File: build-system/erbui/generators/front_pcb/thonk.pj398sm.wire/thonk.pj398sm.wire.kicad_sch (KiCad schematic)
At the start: 4 parts, among them J1 IN

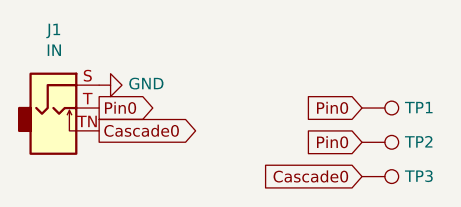
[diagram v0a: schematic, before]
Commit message: Replace cascade feature with normalling feature
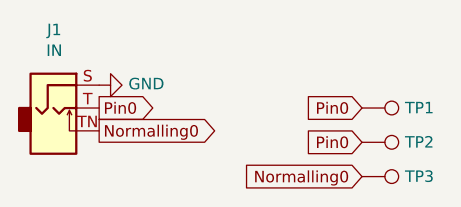
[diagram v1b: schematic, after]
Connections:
- net Cascade0 renamed Normalling0
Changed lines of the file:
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@@
 (kicad_sch (version 20211123) (generator eeschema)
   (paper "A4")
-  (global_label "Cascade0" (shape input) (at 127 114.3 180) (fields_autoplaced)
+  (global_label "Normalling0" (shape input) (at 127 114.3 180) (fields_autoplaced)
     (effects (font (size 1.27 1.27)) (justify right))
-    (property "Intersheet References" "${INTERSHEET_REFS}" (id 0) (at 0 0 0)
-      (effects (font (size 1.27 1.27)) hide)
+    (property "Intersheet References" "${INTERSHEET_REFS}" (id 0) (at 113.1248 114.2206 0)
+      (effects (font (size 1.27 1.27)) (justify right) hide)
     )
   )
@@
     )
   )
-  (global_label "Cascade0" (shape output) (at 97.79 109.22 0) (fields_autoplaced)
+  (global_label "Normalling0" (shape output) (at 97.79 109.22 0) (fields_autoplaced)
     (effects (font (size 1.27 1.27)) (justify left))
-    (property "Intersheet References" "${INTERSHEET_REFS}" (id 0) (at 0 0 0)
-      (effects (font (size 1.27 1.27)) hide)
+    (property "Intersheet References" "${INTERSHEET_REFS}" (id 0) (at 111.6652 109.1406 0)
+      (effects (font (size 1.27 1.27)) (justify left) hide)
     )
   )
